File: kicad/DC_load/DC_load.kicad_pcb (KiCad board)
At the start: 2 copper layers, 110 x 145 mm, 162 parts, among them J1 BNC, J2 red_terminal, J3 red terminal, J4 black terminal, J5 black terminal, J6 USB_B, J8 Conn_01x05_Socket, J9 Conn_01x04_Socket, Q1 MMBT5401, Q3 FQP19N20C, Q4 FQP19N20C, Q5 FQP19N20C, Q6 FQP19N20C, SW1 RotaryEncoder_Switch, SW2 RotaryEncoder_Switch, SW3 SW_Push, SW8 SW_Push, U1 FSA3157P6X, U10 FSA3157P6X, U11 FSA3157P6X, U12 FSA3157P6X, U13 TLV9062, U14 AMS1117-3.3, U15 74HC14D653, U16 93LCxxB, U17 CH340C, U18 TL431DBZ, U2 Screen, U3 NCS21802, U4 NCS21802, U5 TLV9062, U6 TLV9062, U7 LMT84LPM, U8 STM32F103C8Tx, U9 Front plate

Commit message: DC fan boost converter added.
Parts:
- added C54: 10u, Resistor_SMD:R_0805_2012Metric_Pad1.20x1.40mm_HandSolder, F.Cu at (168.8, 170.3)
- added C55: 100n, Capacitor_SMD:C_0603_1608Metric_Pad1.08x0.95mm_HandSolder, F.Cu at (173.3, 174.8)
- added C56: 10u, Resistor_SMD:R_0805_2012Metric_Pad1.20x1.40mm_HandSolder, F.Cu at (168.8, 173.3)
- added C57: 10u, Resistor_SMD:R_0805_2012Metric_Pad1.20x1.40mm_HandSolder, F.Cu at (168.8, 176.2)
- added D5: 1N5819WS, Diode_SMD:D_SOD-323, F.Cu at (164.0, 182.6)
- added J7: Conn_01x04_Socket, Connector_PinSocket_2.54mm:PinSocket_1x04_P2.54mm_Vertical, F.Cu at (164.1, 171.2)
- added L4: 4.7u, Inductor_SMD:L_Bourns_SRN6045TA, F.Cu at (173.3, 156.8)
- added Q13: AO3400A, Package_TO_SOT_SMD:SOT-23, F.Cu at (151.8, 164.1)
- J8: value Conn_01x05_Socket -> FT232 programming port
- moved U9 178.0 mm to (171.0, 55.0)
- moved C29 12.1 mm to (156.3, 151.6)
- moved R29 12.1 mm to (155.6, 139.1)
- moved R30 12.1 mm to (154.0, 141.0)
- moved R32 12.1 mm to (157.2, 139.1)
- moved R33 12.1 mm to (158.8, 141.0)
- moved U13 12.1 mm to (156.4, 147.0)
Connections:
- U15 pad 3: GND -> FAN_BOOST
- U15 pad 4: unconnected-(U15-Pad4) -> Net-(Q13-G)
- U15 pad 5: GND -> FAN_BOOST
- U15 pad 6: unconnected-(U15-Pad6) -> Net-(Q13-G)
- U8 pad 32: unconnected-(U8-PA11-Pad32) -> FAN_BOOST
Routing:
- net /Microcontroller/V_SENSE: track 81.1 -> 97.0 mm
- net /Power_stage/V_SENSE-: track 184.0 -> 171.9 mm
- net /Power_stage/V_SENSE+: track 111.4 -> 99.3 mm
- net FAN_BOOST: track 0.00 -> 3.76 mm, vias 0 -> 2
- net GND: track 104.8 -> 101.0 mm, vias 60 -> 58
- net 5V: vias 8 -> 16
- added copper zone on B.Cu, net 5V

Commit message: Done.
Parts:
- removed J7: Conn_01x04_Socket, Connector_PinSocket_2.54mm:PinSocket_1x04_P2.54mm_Vertical
- added C58: 10u, Capacitor_SMD:C_0603_1608Metric_Pad1.08x0.95mm_HandSolder, F.Cu at (150.7, 145.9)
- added C59: 10u, Capacitor_SMD:C_0603_1608Metric_Pad1.08x0.95mm_HandSolder, F.Cu at (147.3, 145.9)
- added C60: 10u, Capacitor_SMD:C_0603_1608Metric_Pad1.08x0.95mm_HandSolder, F.Cu at (147.3, 147.4)
- added C61: 10u, Capacitor_SMD:C_0603_1608Metric_Pad1.08x0.95mm_HandSolder, F.Cu at (150.5, 160.8)
- added C62: 10u, Capacitor_SMD:C_0603_1608Metric_Pad1.08x0.95mm_HandSolder, F.Cu at (150.5, 162.3)
- added C63: 10u, Capacitor_SMD:C_0603_1608Metric_Pad1.08x0.95mm_HandSolder, F.Cu at (153.9, 162.3)
- added J10: DC fan connector, Connector_PinHeader_2.54mm:PinHeader_1x04_P2.54mm_Vertical, B.Cu at (149.4, 165.0)
- added R64: 10k, Resistor_SMD:R_0603_1608Metric_Pad0.98x0.95mm_HandSolder, F.Cu at (155.4, 167.7)
- added R65: 10k, Resistor_SMD:R_0603_1608Metric_Pad0.98x0.95mm_HandSolder, F.Cu at (151.7, 169.4)
- added R66: 49.9k, Resistor_SMD:R_0603_1608Metric_Pad0.98x0.95mm_HandSolder, F.Cu at (151.7, 167.7)
- added TP1: TestPoint, TestPoint:TestPoint_Pad_D2.0mm, B.Cu at (59.3, 140.5)
- added TP10: TestPoint, TestPoint:TestPoint_Pad_D2.0mm, F.Cu at (94.7, 117.7)
- added TP2: TestPoint, TestPoint:TestPoint_Pad_D2.0mm, B.Cu at (158.1, 184.6)
- added TP3: TestPoint, TestPoint:TestPoint_Pad_D2.0mm, B.Cu at (158.1, 175.0)
- added TP4: TestPoint, TestPoint:TestPoint_Pad_D2.0mm, B.Cu at (155.0, 175.0)
- added TP5: TestPoint, TestPoint:TestPoint_Pad_D2.0mm, B.Cu at (54.0, 140.5)
- added TP6: TestPoint, TestPoint:TestPoint_Pad_D2.0mm, B.Cu at (151.9, 168.3)
- added TP7: TestPoint, TestPoint:TestPoint_Pad_D2.0mm, B.Cu at (148.8, 168.3)
- added TP8: TestPoint, TestPoint:TestPoint_Pad_D2.0mm, F.Cu at (94.7, 111.6)
- added TP9: TestPoint, TestPoint:TestPoint_Pad_D2.0mm, F.Cu at (94.7, 106.7)
- C54, C56, C57: footprint Resistor_SMD:R_0805_2012Metric_Pad1.20x1.40mm_HandSolder -> Capacitor_SMD:C_0603_1608Metric_Pad1.08x0.95mm_HandSolder
- L4: footprint Inductor_SMD:L_Bourns_SRN6045TA -> DC_load:L_Bourns_SRN6045TA; moved to B.Cu
- moved C56 111.9 mm to (59.2, 150.7), turned to 90 degrees
- moved C57 34.0 mm to (150.7, 147.4)
- moved D5 27.4 mm to (151.3, 158.3), turned to 90 degrees
- moved C55 25.2 mm to (153.9, 158.7)
- moved L4 24.8 mm to (149.0, 152.0), turned to -90 degrees
- moved C54 17.7 mm to (153.9, 160.8)
- moved Q13 8.14 mm to (153.3, 156.1), turned to 180 degrees
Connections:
- net Net-(D5-A) renamed /Microcontroller/FAN_DRAIN
- C54 pad 1: GND -> /Microcontroller/FAN_OUT
- C54 pad 2: Net-(D5-K) -> GND
- C55 pad 1: Net-(D5-K) -> /Microcontroller/FAN_OUT
- C56 pad 1: GND -> 5V
- C56 pad 2: 5V -> GND
- C57 pad 1: GND -> 5V
- C57 pad 2: 5V -> GND
- D5 pad 1: Net-(D5-K) -> /Microcontroller/FAN_OUT
- U8 pad 17: CH2_PWM -> FAN_VOLT
- U8 pad 41: ENC_SW_2 -> CH2_PWM
- U8 pad 45: unconnected-(U8-PB8-Pad45) -> ENC_SW_2
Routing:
- net FAN_BOOST: track 3.76 -> 68.5 mm, vias 2 -> 3
- net FAN_VOLT: track 0.00 -> 62.5 mm, vias 0 -> 3
- net Net-(Q13-G): track 0.00 -> 41.5 mm, vias 0 -> 2
- net GND: track 101.0 -> 112.6 mm, vias 58 -> 72
- net CH2_PWM: track 61.7 -> 54.9 mm
- net /Microcontroller/CH1_MEAS: track 150.2 -> 156.9 mm
- net 3V3: track 122.0 -> 126.0 mm, vias 22 -> 27
- net /Microcontroller/CH4_MEAS: track 156.4 -> 160.2 mm
- net Net-(R27-Pad2): track 102.2 -> 105.9 mm
- net Net-(R25-Pad2): track 102.6 -> 106.3 mm
- net /Microcontroller/CH3_MEAS: track 151.0 -> 154.6 mm
- net /Microcontroller/FAN_OUT: track 0.00 -> 3.00 mm
- net TACH: track 0.00 -> 2.73 mm
- net CH1_CONTROL: track 13.8 -> 16.5 mm
- net Net-(R22-Pad2): track 173.5 -> 175.0 mm
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- added copper zone on F.Cu, net /Microcontroller/FAN_DRAIN
- added copper zone on F.Cu, net /Microcontroller/FAN_OUT
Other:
- board text added: "5V"
- board text added: "GND"

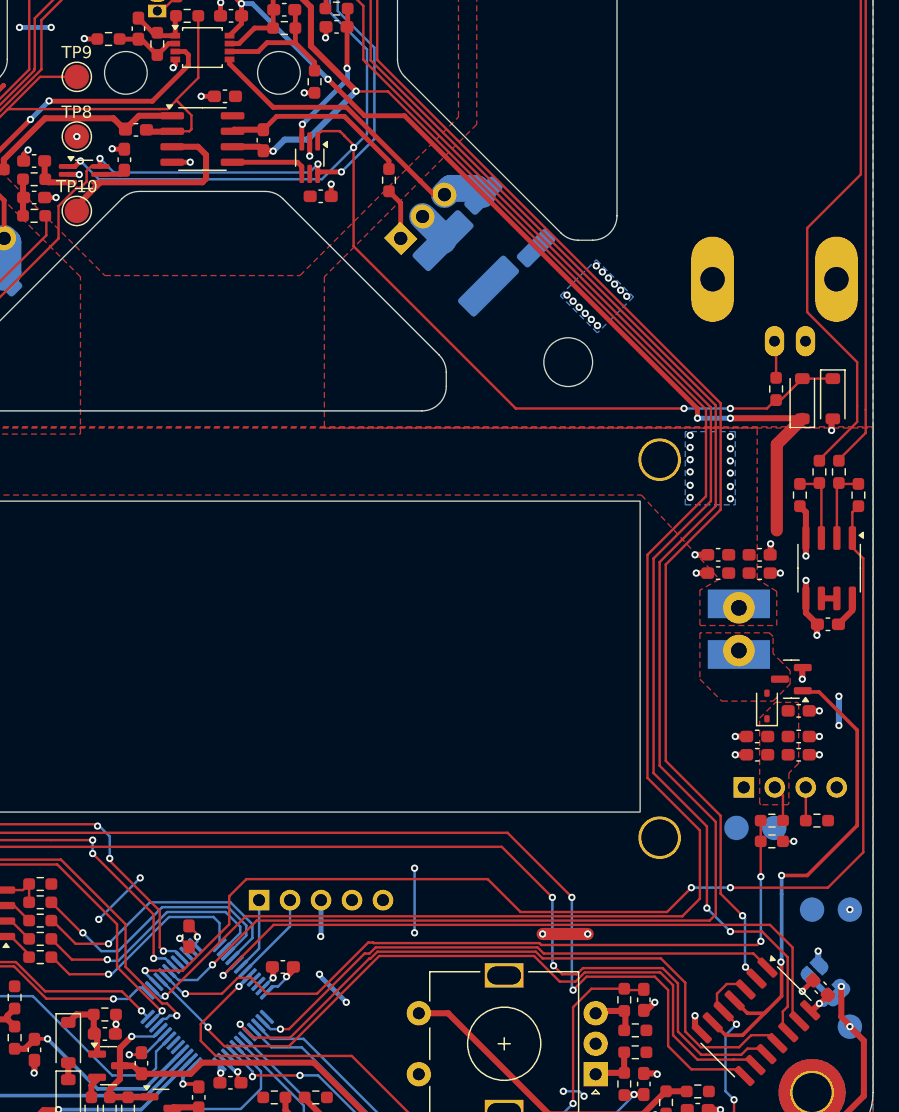
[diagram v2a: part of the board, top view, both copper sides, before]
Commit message: No errors, fan added.
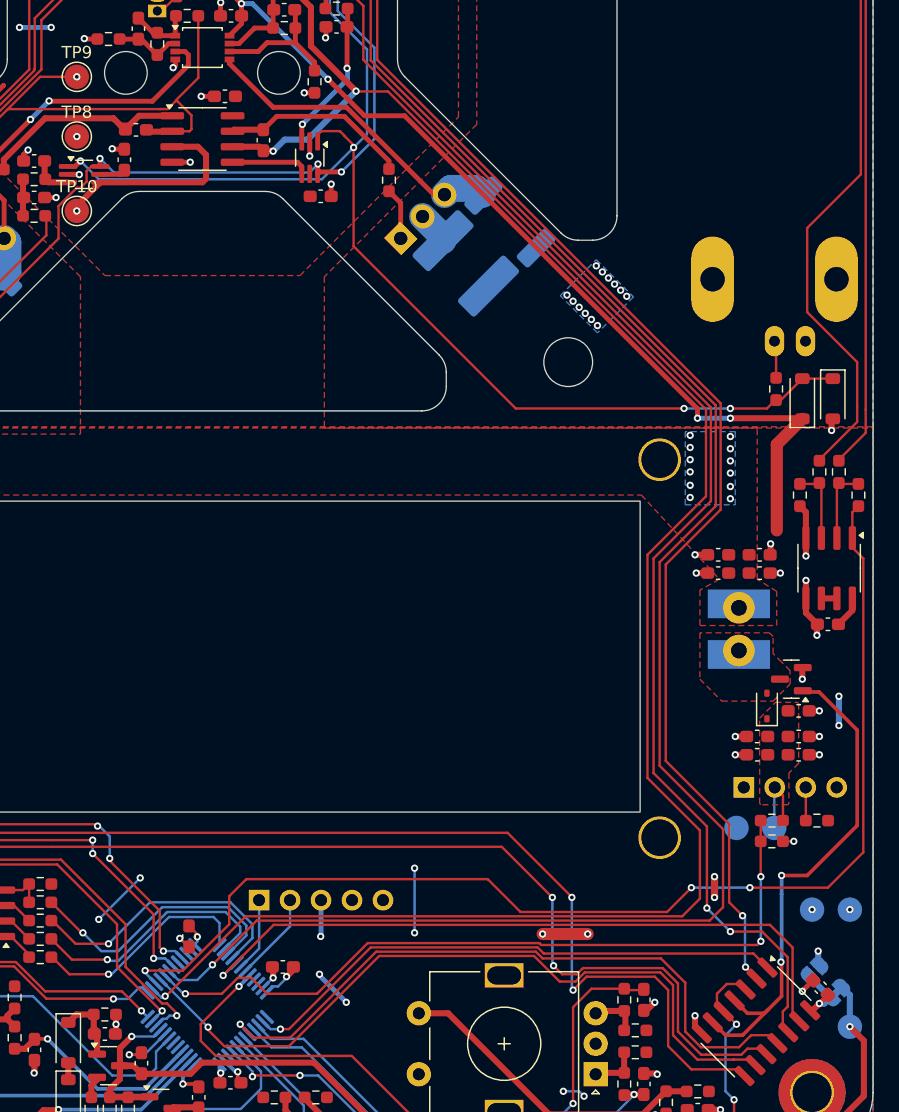
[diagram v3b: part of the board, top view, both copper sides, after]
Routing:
- net /Microcontroller/FAN_OUT: track 3.00 -> 6.34 mm
- net GND: track 112.6 -> 114.3 mm, vias 72 -> 75
- net VREF: track 87.8 -> 87.5 mm, vias 3 -> 2
- net CH1_CONTROL: vias 0 -> 1
- net /Microcontroller/CH1_MEAS: vias 3 -> 4

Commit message: Review left.
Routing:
- net 3V3: track 126.0 -> 141.8 mm, vias 27 -> 29
- net GND: track 114.3 -> 124.0 mm, vias 75 -> 81
- net 5V: track 160.3 -> 160.9 mm

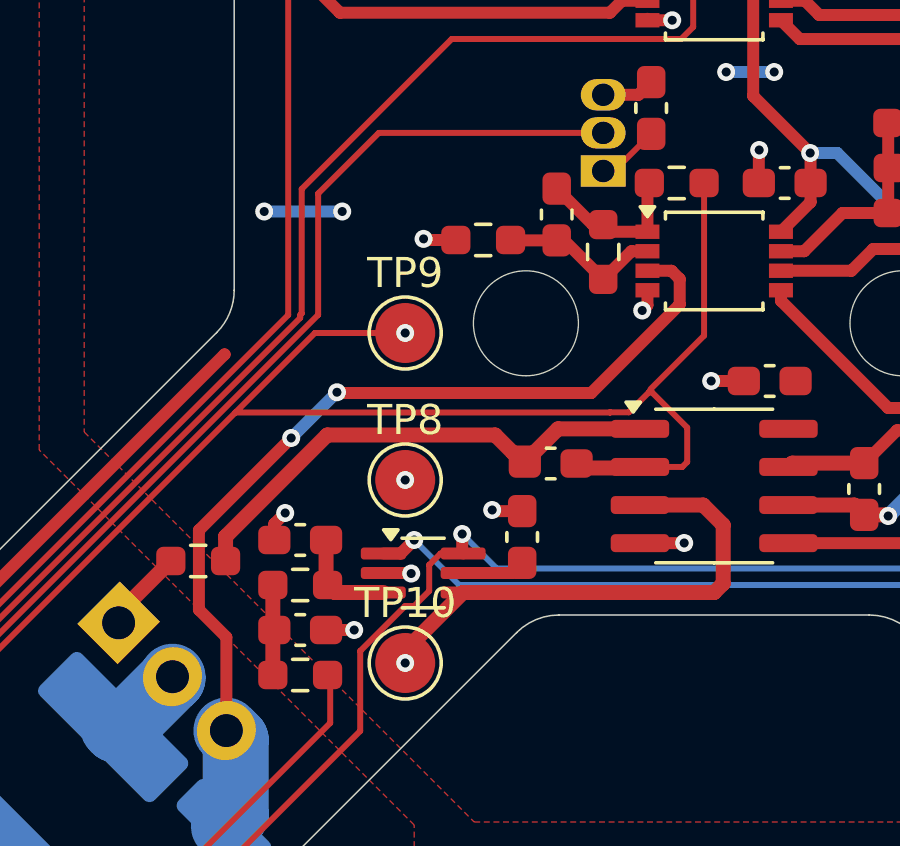
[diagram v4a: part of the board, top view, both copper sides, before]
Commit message: Added jumper.
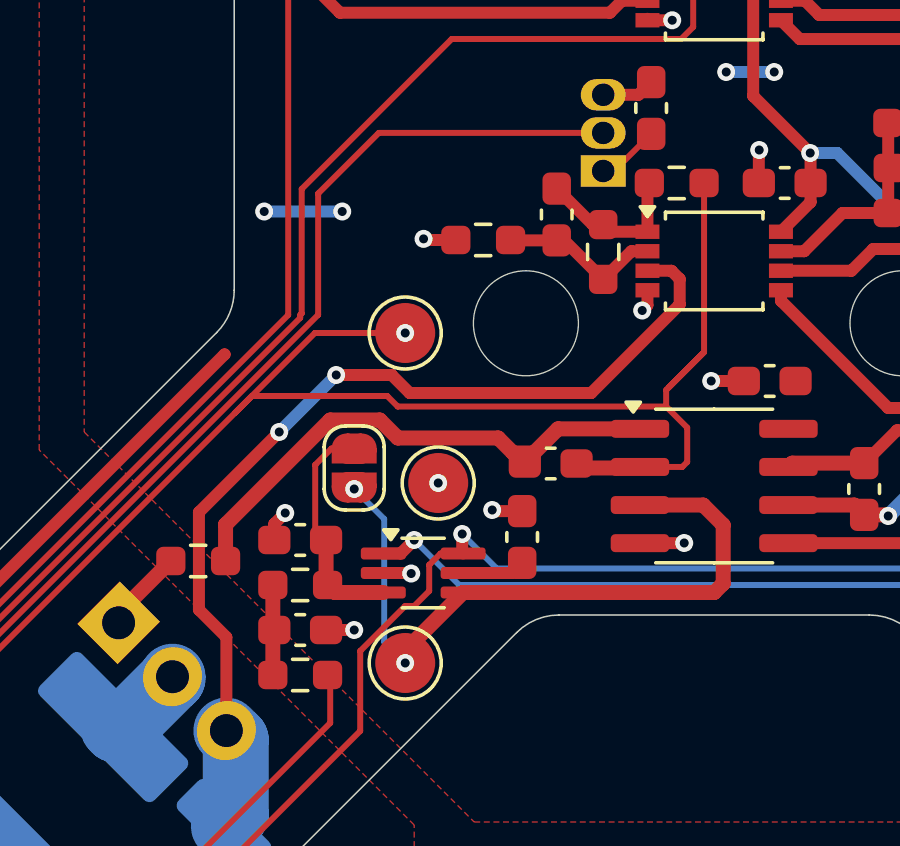
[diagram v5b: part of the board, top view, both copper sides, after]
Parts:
- added JP3: Jumper_2_Open, Jumper:SolderJumper-2_P1.3mm_Open_RoundedPad1.0x1.5mm, F.Cu at (93.0, 111.2)
- moved TP8 1.10 mm to (95.8, 111.7)
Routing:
- net CH1_CONTROL: track 16.5 -> 23.1 mm, vias 1 -> 2
- net Net-(JP3-A): track 3.48 -> 7.61 mm
- net /Microcontroller/CH1_MEAS: track 156.9 -> 158.8 mm
- net Net-(Q3-S): track 31.7 -> 32.6 mm
- net Net-(C20-Pad2): track 16.6 -> 17.3 mm

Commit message: More agresive PWM filtering.
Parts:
- C21, C23, C25, C27: value 10n -> 10u
- C22, C24, C26, C28: value 100p -> 100n
- turned C21 to 0 degrees
- turned C23 to 180 degrees
- turned C25 to 0 degrees
- turned C27 to 180 degrees
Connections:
- C21 pad 1: GND -> Net-(C21-Pad1)
- C21 pad 2: Net-(C21-Pad2) -> GND
- C23 pad 1: GND -> Net-(C23-Pad1)
- C23 pad 2: Net-(C23-Pad2) -> GND
- C25 pad 1: GND -> Net-(C25-Pad1)
- C25 pad 2: Net-(C25-Pad2) -> GND
- C27 pad 1: GND -> Net-(C27-Pad1)
- C27 pad 2: Net-(C27-Pad2) -> GND
- R21 pad 2: Net-(C21-Pad2) -> Net-(C21-Pad1)
- R22 pad 1: Net-(C21-Pad2) -> Net-(C21-Pad1)
- R23 pad 1: Net-(C23-Pad2) -> Net-(C23-Pad1)
- R24 pad 2: Net-(C23-Pad2) -> Net-(C23-Pad1)
- R25 pad 1: Net-(C25-Pad2) -> Net-(C25-Pad1)
- R26 pad 2: Net-(C25-Pad2) -> Net-(C25-Pad1)
- R27 pad 1: Net-(C27-Pad2) -> Net-(C27-Pad1)
- R28 pad 2: Net-(C27-Pad2) -> Net-(C27-Pad1)
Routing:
- net Net-(C23-Pad2): track 3.92 -> 0.00 mm
- net Net-(C23-Pad1): track 0.00 -> 3.92 mm
- net Net-(C25-Pad2): track 3.02 -> 0.00 mm
- net Net-(C25-Pad1): track 0.00 -> 3.02 mm
- net Net-(C27-Pad2): track 3.00 -> 0.00 mm
- net Net-(C27-Pad1): track 0.00 -> 3.00 mm
- net Net-(C21-Pad2): track 3.00 -> 0.00 mm
- net Net-(C21-Pad1): track 0.00 -> 3.00 mm
